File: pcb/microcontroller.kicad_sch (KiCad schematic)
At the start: 24 parts, among them J1 TC2030, J3 TC2030, U3 74HCT541, U4 STM32F103C8T6, U5 SN65HVD230, Y1 8MHz

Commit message: Added part numbers for assembly
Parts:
- C16, C19: LCSC (none) -> C1570
- D7: LCSC (none) -> C151237
- R5, R6: LCSC (none) -> C441730
- U3: LCSC (none) -> C6758
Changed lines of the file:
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@@
+      (effects (font (size 1.27 1.27)) hide)
+    )
+    (property "LCSC" "C151237" (id 4) (at 236.22 124.46 0)
       (effects (font (size 1.27 1.27)) hide)
     )
@@
       (effects (font (size 1.27 1.27)) hide)
     )
+    (property "LCSC" "C441730" (id 4) (at 212.09 119.38 0)
+      (effects (font (size 1.27 1.27)) hide)
+    )
     (pin "1")
     (pin "2")
@@
     )
     (property "Datasheet" "http://www.ti.com/lit/gpn/sn74HCT541" (id 3) (at 245.11 60.96 0)
+      (effects (font (size 1.27 1.27)) hide)
+    )
+    (property "LCSC" "C6758" (id 4) (at 245.11 60.96 0)
       (effects (font (size 1.27 1.27)) hide)
     )
@@
       (effects (font (size 1.27 1.27)) hide)
     )
+    (property "LCSC" "C1570" (id 4) (at 236.22 110.49 0)
+      (effects (font (size 1.27 1.27)) hide)
+    )
     (pin "1")
     (pin "2")
@@
     )
     (property "Datasheet" "~" (id 3) (at 236.22 138.43 0)
+      (effects (font (size 1.27 1.27)) hide)
+    )
+    (property "LCSC" "C1570" (id 4) (at 236.22 138.43 0)
       (effects (font (size 1.27 1.27)) hide)
     )
@@
       (effects (font (size 1.27 1.27)) hide)
     )
+    (property "LCSC" "C441730" (id 4) (at 212.09 129.54 0)
+      (effects (font (size 1.27 1.27)) hide)
+    )

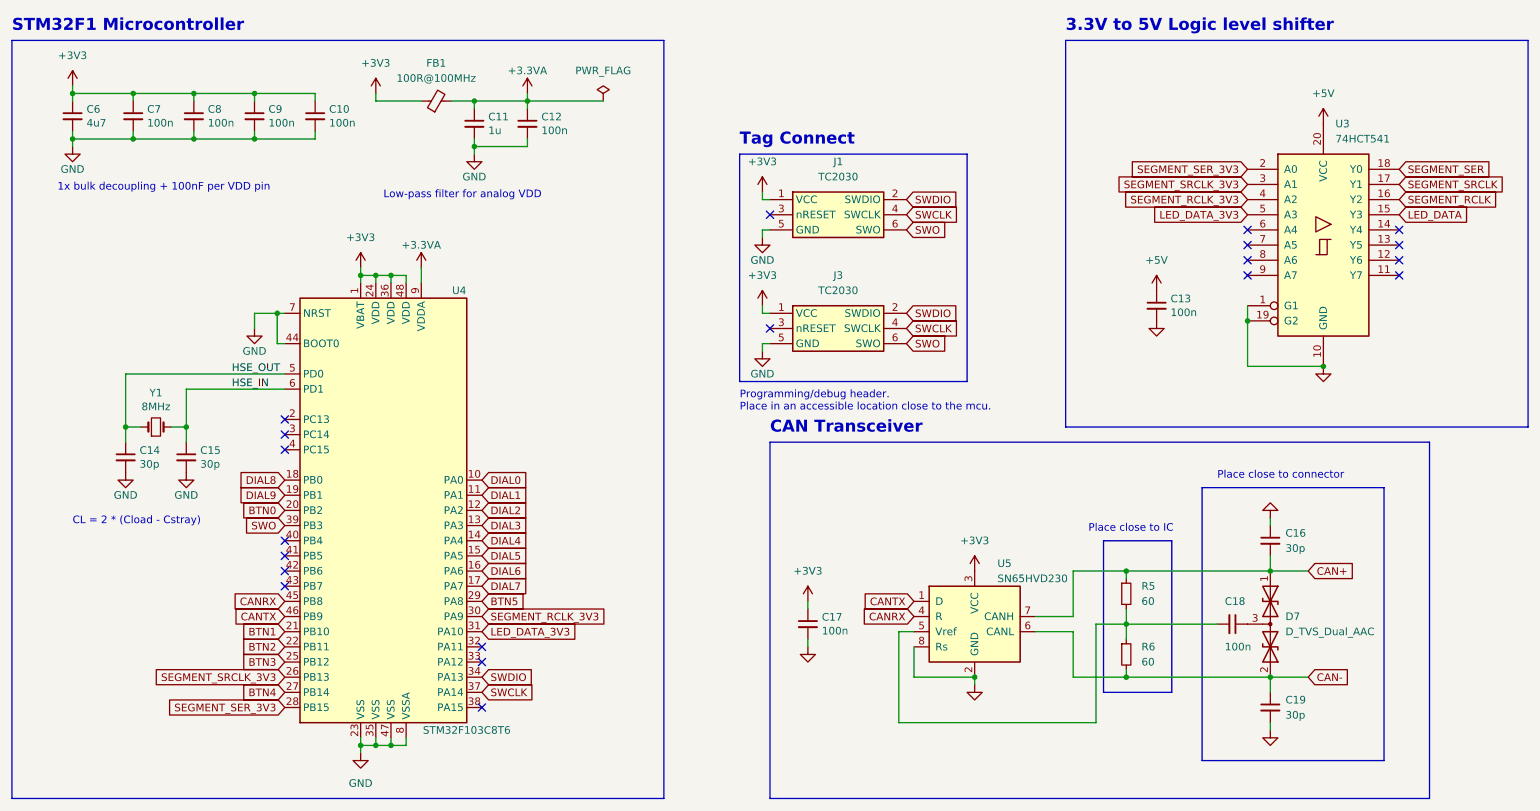
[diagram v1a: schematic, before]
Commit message: Started work on discrete led displays
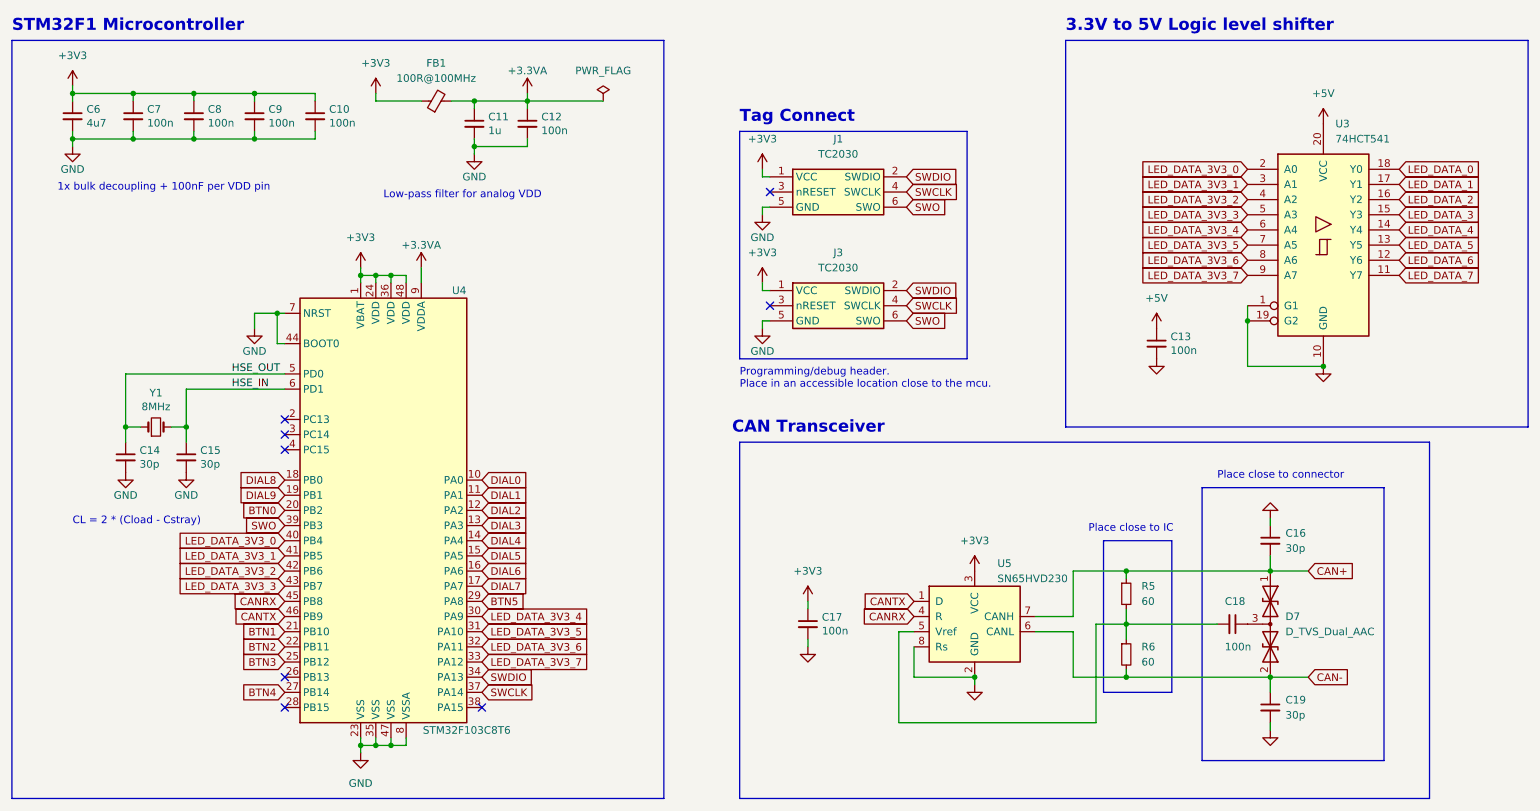
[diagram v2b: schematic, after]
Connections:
- net LED_DATA_7: now reaches U3.11 (Y7)
- net LED_DATA_6: now reaches U3.12 (Y6)
- net LED_DATA_5: now reaches U3.13 (Y5)
- net LED_DATA_4: now reaches U3.14 (Y4)
- net LED_DATA_3V3_4: now reaches U3.6 (A4)
- net LED_DATA_3V3_4: now also U4.30 (PA9)
- net LED_DATA_3V3_5: now reaches U3.7 (A5)
- net LED_DATA_3V3_5: now also U4.31 (PA10)
- net LED_DATA_3V3_6: now reaches U3.8 (A6)
- net LED_DATA_3V3_6: now also U4.32 (PA11)
- net LED_DATA_3V3_7: now reaches U3.9 (A7)
- net LED_DATA_3V3_7: now also U4.33 (PA12)
- net LED_DATA_3V3_0: now reaches U4.40 (PB4)
- net LED_DATA_3V3_0: now also U3.2 (A0)
- net LED_DATA_3V3_1: now reaches U4.41 (PB5)
- net LED_DATA_3V3_1: now also U3.3 (A1)
- net LED_DATA_3V3_2: now reaches U4.42 (PB6)
- net LED_DATA_3V3_2: now also U3.4 (A2)
- net LED_DATA_3V3_3: now reaches U4.43 (PB7)
- net LED_DATA_3V3_3: now also U3.5 (A3)
- net LED_DATA renamed LED_DATA_3
- removed net LED_DATA_3V3: U3.5 (A3), U4.31 (PA10)
- net SEGMENT_RCLK renamed LED_DATA_2
- removed net SEGMENT_RCLK_3V3: U3.4 (A2), U4.30 (PA9)
- net SEGMENT_SER renamed LED_DATA_0
- net SEGMENT_SER_3V3: no longer names the net of U4.28 (PB15)
- net SEGMENT_SER_3V3: no longer U3.2 (A0)
- net SEGMENT_SRCLK renamed LED_DATA_1
- net SEGMENT_SRCLK_3V3: no longer names the net of U4.26 (PB13)
- net SEGMENT_SRCLK_3V3: no longer U3.3 (A1)
- no-connect marks 20 -> 8
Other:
- moved on the sheet: C13, J1, J3

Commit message: PCB layout work
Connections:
- net LED_DATA_3V3_0: now also U4.43 (PB7); no longer U4.40 (PB4)
- net LED_DATA_3V3_1: now also U4.42 (PB6); no longer U4.41 (PB5)
- net LED_DATA_3V3_2: now also U4.41 (PB5); no longer U4.42 (PB6)
- net LED_DATA_3V3_3: now also U4.40 (PB4); no longer U4.43 (PB7)
- net LED_DATA_3V3_4: now also U4.33 (PA12); no longer U4.30 (PA9)
- net LED_DATA_3V3_5: now also U4.32 (PA11); no longer U4.31 (PA10)
- net LED_DATA_3V3_6: now also U4.31 (PA10); no longer U4.32 (PA11)
- net LED_DATA_3V3_7: now also U4.30 (PA9); no longer U4.33 (PA12)
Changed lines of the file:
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@@
     )
   )
-  (global_label "LED_DATA_3V3_7" (shape input) (at 104.14 130.81 0) (fields_autoplaced)
-    (effects (font (size 1.27 1.27)) (justify left))
-    (property "Intersheet References" "${INTERSHEET_REFS}" (id 0) (at 122.035 130.7306 0)
+  (global_label "LED_DATA_3V3_7" (shape input) (at 104.14 123.19 0) (fields_autoplaced)
+    (effects (font (size 1.27 1.27)) (justify left))
+    (property "Intersheet References" "${INTERSHEET_REFS}" (id 0) (at 122.035 123.2694 0)
       (effects (font (size 1.27 1.27)) (justify left) hide)
     )
@@
     )
   )
-  (global_label "LED_DATA_3V3_3" (shape input) (at 71.12 118.11 180) (fields_autoplaced)
-    (effects (font (size 1.27 1.27)) (justify right))
-    (property "Intersheet References" "${INTERSHEET_REFS}" (id 0) (at 53.225 118.0306 0)
+  (global_label "LED_DATA_3V3_3" (shape input) (at 71.12 110.49 180) (fields_autoplaced)
+    (effects (font (size 1.27 1.27)) (justify right))
+    (property "Intersheet References" "${INTERSHEET_REFS}" (id 0) (at 53.225 110.5694 0)
       (effects (font (size 1.27 1.27)) (justify right) hide)
     )
@@
     )
   )
-  (global_label "LED_DATA_3V3_0" (shape input) (at 71.12 110.49 180) (fields_autoplaced)
-    (effects (font (size 1.27 1.27)) (justify right))
-    (property "Intersheet References" "${INTERSHEET_REFS}" (id 0) (at 53.225 110.4106 0)
+  (global_label "LED_DATA_3V3_0" (shape input) (at 71.12 118.11 180) (fields_autoplaced)
+    (effects (font (size 1.27 1.27)) (justify right))
+    (property "Intersheet References" "${INTERSHEET_REFS}" (id 0) (at 53.225 118.1894 0)
       (effects (font (size 1.27 1.27)) (justify right) hide)
     )
@@
     )
   )
-  (global_label "LED_DATA_3V3_5" (shape input) (at 104.14 125.73 0) (fields_autoplaced)
-    (effects (font (size 1.27 1.27)) (justify left))
-    (property "Intersheet References" "${INTERSHEET_REFS}" (id 0) (at 122.035 125.6506 0)
+  (global_label "LED_DATA_3V3_5" (shape input) (at 104.14 128.27 0) (fields_autoplaced)
+    (effects (font (size 1.27 1.27)) (justify left))
+    (property "Intersheet References" "${INTERSHEET_REFS}" (id 0) (at 122.035 128.3494 0)
       (effects (font (size 1.27 1.27)) (justify left) hide)
     )
@@
     )
   )
-  (global_label "LED_DATA_3V3_6" (shape input) (at 104.14 128.27 0) (fields_autoplaced)
-    (effects (font (size 1.27 1.27)) (justify left))
-    (property "Intersheet References" "${INTERSHEET_REFS}" (id 0) (at 122.035 128.1906 0)
+  (global_label "LED_DATA_3V3_6" (shape input) (at 104.14 125.73 0) (fields_autoplaced)
+    (effects (font (size 1.27 1.27)) (justify left))
+    (property "Intersheet References" "${INTERSHEET_REFS}" (id 0) (at 122.035 125.8094 0)
       (effects (font (size 1.27 1.27)) (justify left) hide)
     )
@@
     )
   )
-  (global_label "LED_DATA_3V3_1" (shape input) (at 71.12 113.03 180) (fields_autoplaced)
-    (effects (font (size 1.27 1.27)) (justify right))
-    (property "Intersheet References" "${INTERSHEET_REFS}" (id 0) (at 53.225 112.9506 0)
-      (effects (font (size 1.27 1.27)) (justify right) hide)
-    )
-  )
-  (global_label "LED_DATA_3V3_4" (shape input) (at 104.14 123.19 0) (fields_autoplaced)
-    (effects (font (size 1.27 1.27)) (justify left))
-    (property "Intersheet References" "${INTERSHEET_REFS}" (id 0) (at 122.035 123.1106 0)
+  (global_label "LED_DATA_3V3_1" (shape input) (at 71.12 115.57 180) (fields_autoplaced)
+    (effects (font (size 1.27 1.27)) (justify right))
+    (property "Intersheet References" "${INTERSHEET_REFS}" (id 0) (at 53.225 115.6494 0)
+      (effects (font (size 1.27 1.27)) (justify right) hide)
+    )
+  )
+  (global_label "LED_DATA_3V3_4" (shape input) (at 104.14 130.81 0) (fields_autoplaced)
+    (effects (font (size 1.27 1.27)) (justify left))
+    (property "Intersheet References" "${INTERSHEET_REFS}" (id 0) (at 122.035 130.8894 0)
       (effects (font (size 1.27 1.27)) (justify left) hide)
     )
@@
     )
   )
-  (global_label "LED_DATA_3V3_2" (shape input) (at 71.12 115.57 180) (fields_autoplaced)
-    (effects (font (size 1.27 1.27)) (justify right))
-    (property "Intersheet References" "${INTERSHEET_REFS}" (id 0) (at 53.225 115.4906 0)
-      (effects (font (size 1.27 1.27)) (justify right) hide)
-    )
+  (global_label "LED_DATA_3V3_2" (shape input) (at 71.12 113.03 180) (fields_autoplaced)
+    (effects (font (size 1.27 1.27)) (justify right))
+    (property "Intersheet References" "${INTERSHEET_REFS}" (id 0) (at 53.225 113.1094 0)
+      (effects (font (size 1.27 1.27)) (justify right) hide)
+    )

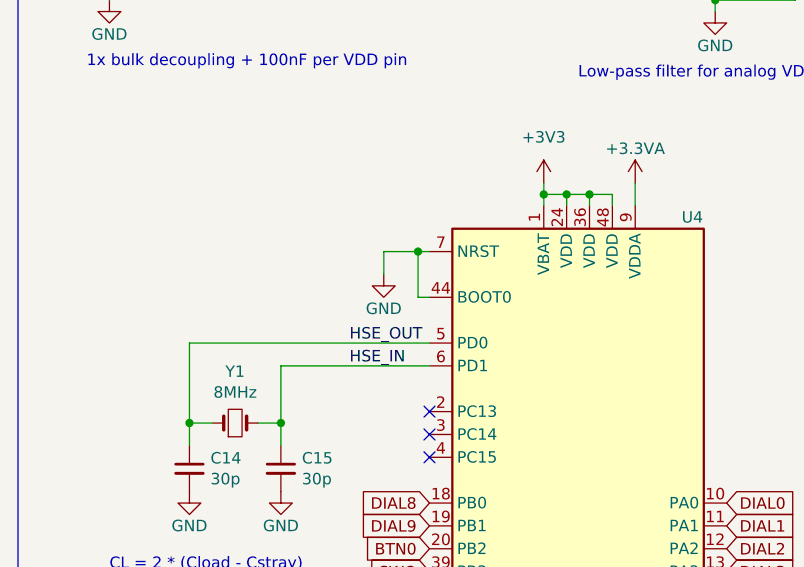
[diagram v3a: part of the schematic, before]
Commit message: Fix PCB, use DMA for ws2812 LEDs (#5)
* Disconnected NRESET

* Firmware work

* Added dial input on ADC0/1

* Added CAN reading

* Send dials over CAN to ecu

* Switch to DMA for WS2812 control

---------

Co-authored-by: Noah-Gould <74689929+Noah-Gould@users.noreply.github.com>
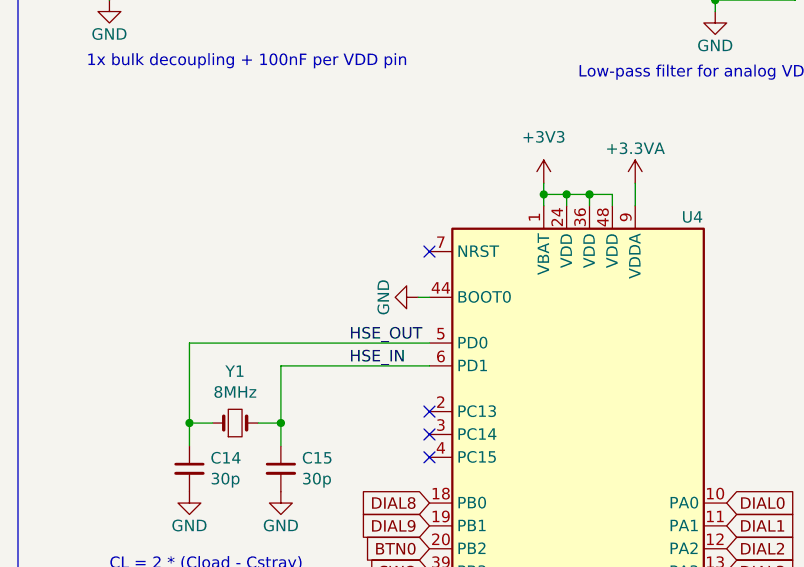
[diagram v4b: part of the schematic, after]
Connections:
- net GND: no longer U4.7 (NRST)
- no-connect marks 8 -> 9
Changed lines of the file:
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@@
     (title "STM32F103 MICROCONTROLLER")
-  )
-  (junction (at 69.85 72.39) (diameter 0) (color 0 0 0 0)
   )
   (junction (at 212.09 115.57) (diameter 0) (color 0 0 0 0)
@@
   (no_connect (at 152.4 52.07))
   (no_connect (at 71.12 138.43))
+  (no_connect (at 71.12 72.39))
   (no_connect (at 104.14 138.43))
   (no_connect (at 71.12 133.35))
@@
     (stroke (width 0) (type default) (color 0 0 0 0))
   )
-  (wire (pts (xy 69.85 72.39) (xy 71.12 72.39))
-    (stroke (width 0) (type default) (color 0 0 0 0))
-  )
   (wire (pts (xy 242.57 133.35) (xy 236.22 133.35))
     (stroke (width 0) (type default) (color 0 0 0 0))
@@
     (stroke (width 0) (type default) (color 0 0 0 0))
   )
-  (wire (pts (xy 69.85 77.47) (xy 69.85 72.39))
-    (stroke (width 0) (type default) (color 0 0 0 0))
-  )
   (wire (pts (xy 66.04 43.18) (xy 76.2 43.18))
     (stroke (width 0) (type default) (color 0 0 0 0))
@@
     (stroke (width 0) (type default) (color 0 0 0 0))
   )
-  (wire (pts (xy 66.04 72.39) (xy 66.04 74.93))
-    (stroke (width 0) (type default) (color 0 0 0 0))
-  )
   (wire (pts (xy 236.22 115.57) (xy 236.22 113.03))
     (stroke (width 0) (type default) (color 0 0 0 0))
@@
   )
   (polyline (pts (xy 255.27 147.32) (xy 224.79 147.32))
-    (stroke (width 0) (type default) (color 0 0 0 0))
-  )
-  (wire (pts (xy 69.85 72.39) (xy 66.04 72.39))
     (stroke (width 0) (type default) (color 0 0 0 0))
   )
@@
     (pin "2")
   )
-  (symbol (lib_id "power:GND") (at 66.04 74.93 0) (unit 1)
-    (in_bom yes) (on_board yes)
-    (property "Reference" "#PWR030" (id 0) (at 66.04 81.28 0)
-      (effects (font (size 1.27 1.27)) hide)
-    )
-    (property "Value" "GND" (id 1) (at 66.04 78.74 0))
-    (property "Footprint" "" (id 2) (at 66.04 74.93 0)
-      (effects (font (size 1.27 1.27)) hide)
-    )
-    (property "Datasheet" "" (id 3) (at 66.04 74.93 0)
-      (effects (font (size 1.27 1.27)) hide)
-    )
+  (symbol (lib_id "power:GND") (at 69.85 77.47 270) (unit 1)
+    (in_bom yes) (on_board yes)
+    (property "Reference" "#PWR030" (id 0) (at 63.5 77.47 0)
+      (effects (font (size 1.27 1.27)) hide)
+    )
+    (property "Value" "GND" (id 1) (at 66.04 77.47 0))
+    (property "Footprint" "" (id 2) (at 69.85 77.47 0)
+      (effects (font (size 1.27 1.27)) hide)
+    )
+    (property "Datasheet" "" (id 3) (at 69.85 77.47 0)
+      (effects (font (size 1.27 1.27)) hide)
+    )

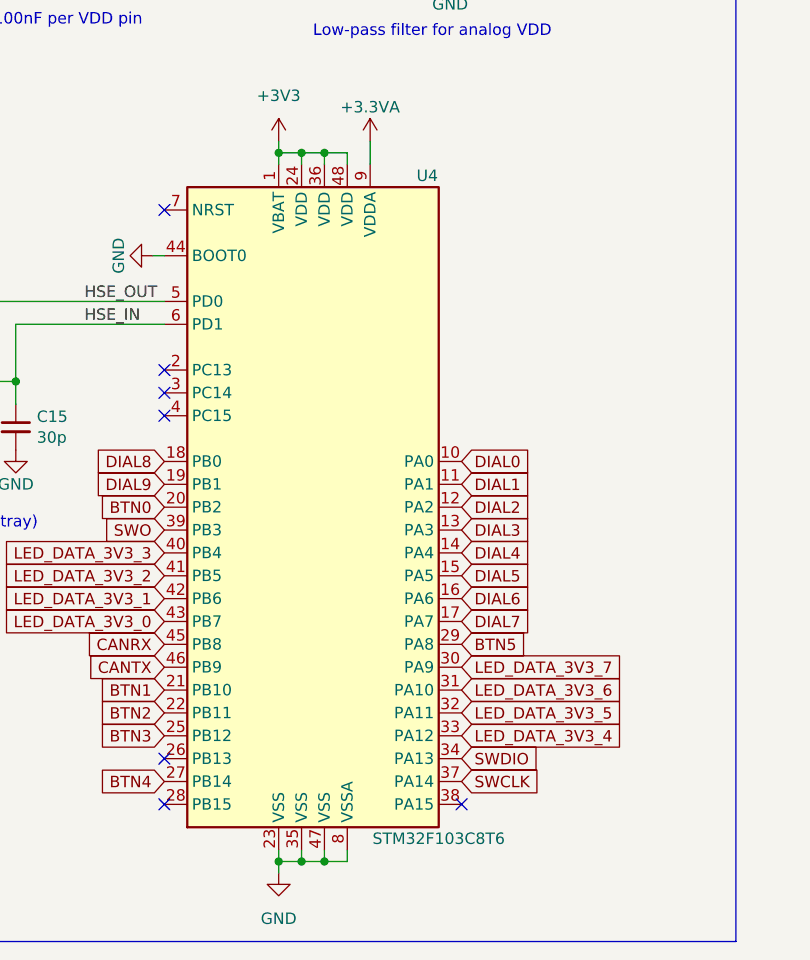
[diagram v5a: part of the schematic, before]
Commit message: Fix kikad 7 schematic issues
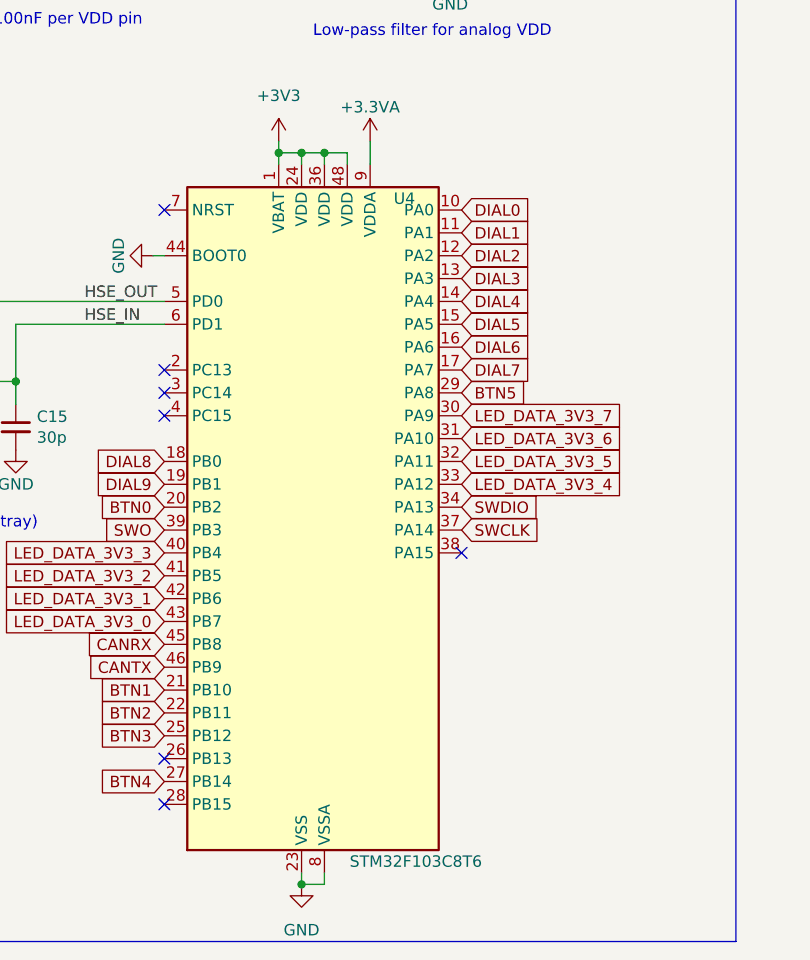
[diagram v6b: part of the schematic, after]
